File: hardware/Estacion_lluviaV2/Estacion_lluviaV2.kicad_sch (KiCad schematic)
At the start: 0 parts

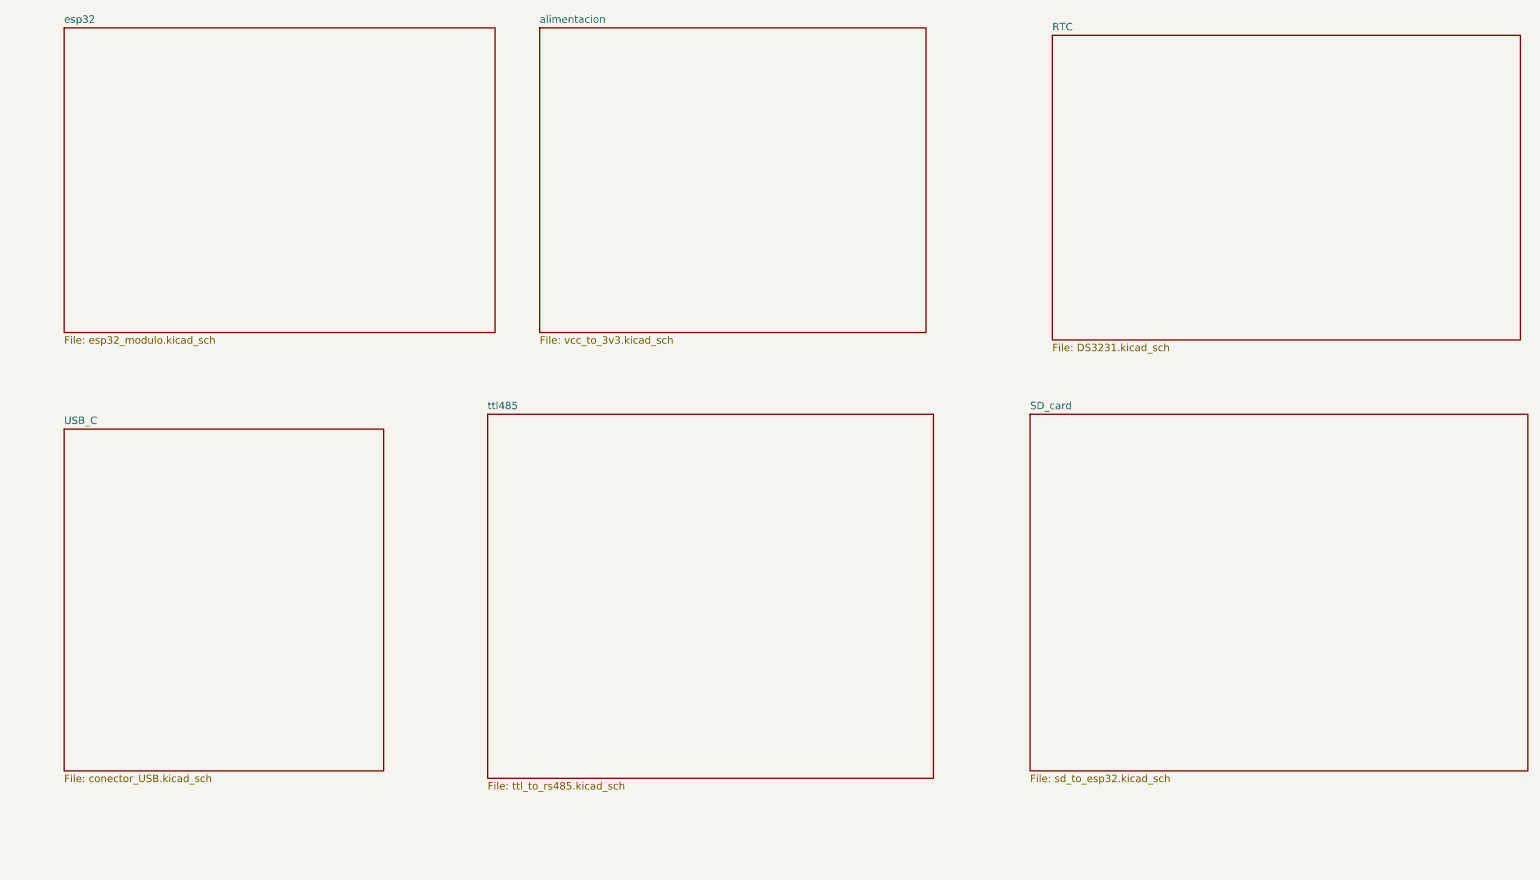
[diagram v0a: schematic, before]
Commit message: Se agregaron nuevos archivos
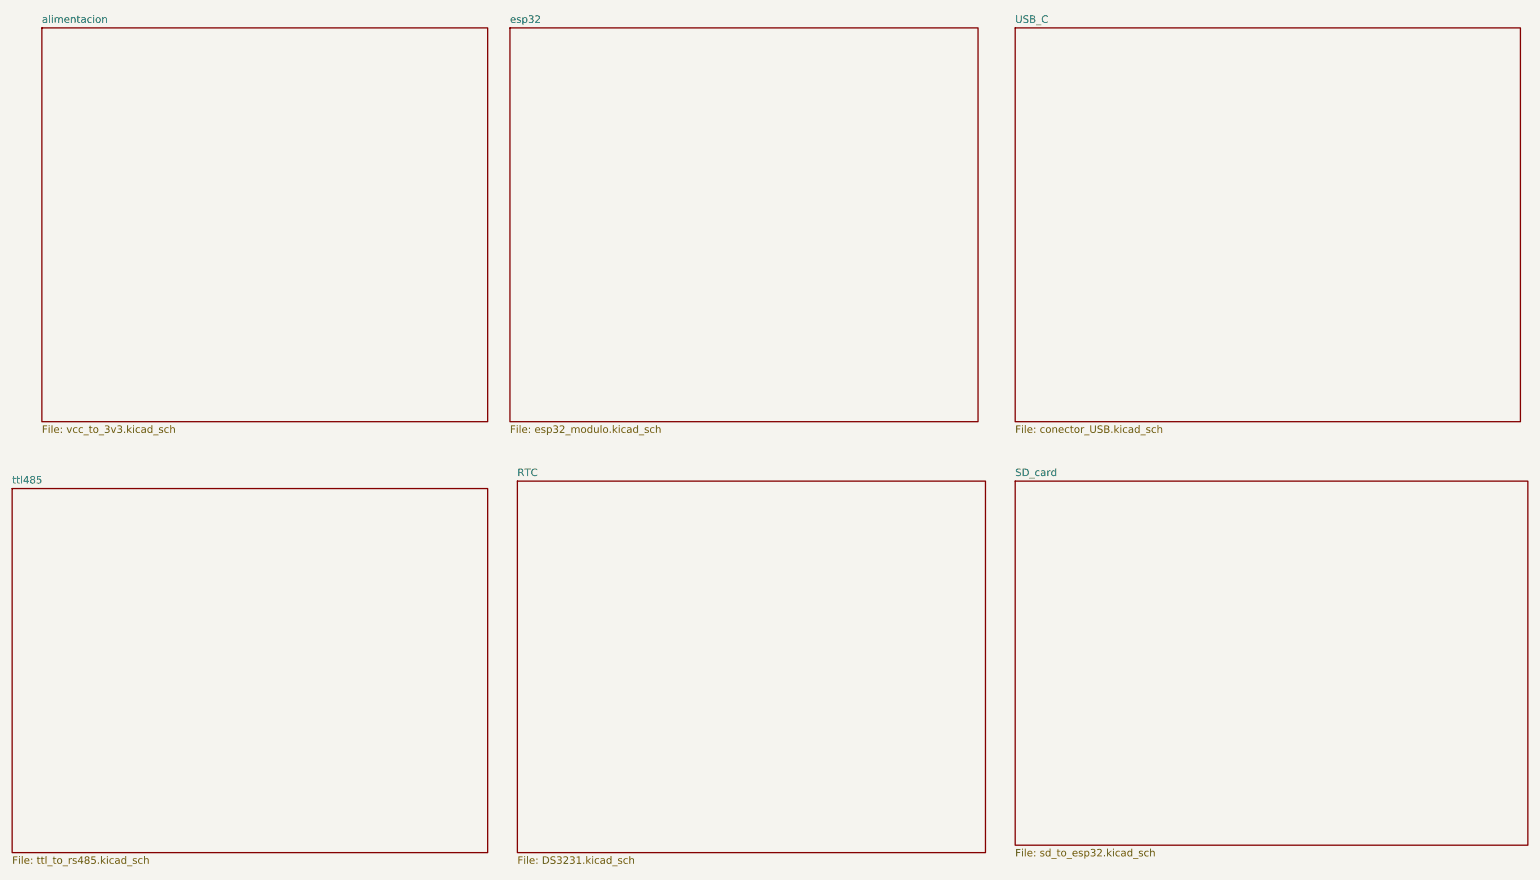
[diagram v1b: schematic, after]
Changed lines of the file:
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@@
 	(paper "A4")
 	(sheet
-		(at 22.86 88.9)
-		(size 54.61 58.42)
+		(at 185.42 20.32)
+		(size 86.36 67.31)
 		(exclude_from_sim no)
 		(in_bom yes)
@@
 		)
 		(property "Sheetname" "USB_C"
-			(at 22.86 88.1884 0)
+			(at 185.42 19.6084 0)
 			(effects
 				(font
@@
 		)
 		(property "Sheetfile" "conector_USB.kicad_sch"
-			(at 22.86 147.9046 0)
+			(at 185.42 88.2146 0)
 			(effects
 				(font
@@
 		)
 		(property "Field2" ""
-			(at 22.86 88.9 0)
+			(at 185.42 20.32 0)
 			(effects
 				(font
@@
 		)
 		(instances
-			(project "Estacion_lluvia"
+			(project "Estacion_lluviaV2"
+				(path "/9827a92f-f203-4536-a02d-33745fae0e99"
+					(page "4")
+				)
+			)
+		)
+	)
+	(sheet
+		(at 185.42 97.79)
+		(size 87.63 62.23)
+		(exclude_from_sim no)
+		(in_bom yes)
+		(on_board yes)
+		(dnp no)
+		(fields_autoplaced yes)
+		(stroke
+			(width 0.1524)
+			(type solid)
+		)
+		(fill
+			(color 0 0 0 0.0000)
+		)
+		(property "Sheetname" "SD_card"
+			(at 185.42 97.0784 0)
+			(effects
+				(font
+					(size 1.27 1.27)
+				)
+				(justify left bottom)
+			)
+		)
+		(property "Sheetfile" "sd_to_esp32.kicad_sch"
+			(at 185.42 160.6046 0)
+			(effects
+				(font
+					(size 1.27 1.27)
+				)
+				(justify left top)
+			)
+		)
+		(instances
+			(project "Estacion_lluviaV2"
 				(path "/9827a92f-f203-4536-a02d-33745fae0e99"
 					(page "7")
@@
 	)
 	(sheet
-		(at 187.96 86.36)
-		(size 85.09 60.96)
-		(exclude_from_sim no)
-		(in_bom yes)
-		(on_board yes)
-		(dnp no)
-		(fields_autoplaced yes)
-		(stroke
-			(width 0.1524)
-			(type solid)
-		)
-		(fill
-			(color 0 0 0 0.0000)
-		)
-		(property "Sheetname" "SD_card"
-			(at 187.96 85.6484 0)
-			(effects
-				(font
-					(size 1.27 1.27)
-				)
-				(justify left bottom)
-			)
-		)
-		(property "Sheetfile" "sd_to_esp32.kicad_sch"
-			(at 187.96 147.9046 0)
-			(effects
-				(font
-					(size 1.27 1.27)
-				)
-				(justify left top)
-			)
-		)
-		(instances
-			(project "Estacion_lluvia"
+		(at 99.06 20.32)
+		(size 80.01 67.31)
+		(exclude_from_sim no)
+		(in_bom yes)
+		(on_board yes)
+		(dnp no)
+		(fields_autoplaced yes)
+		(stroke
+			(width 0.1524)
+			(type solid)
+		)
+		(fill
+			(color 0 0 0 0.0000)
+		)
+		(property "Sheetname" "esp32"
+			(at 99.06 19.6084 0)
+			(effects
+				(font
+					(size 1.27 1.27)
+				)
+				(justify left bottom)
+			)
+		)
+		(property "Sheetfile" "esp32_modulo.kicad_sch"
+			(at 99.06 88.2146 0)
+			(effects
+				(font
+					(size 1.27 1.27)
+				)
+				(justify left top)
+			)
+		)
+		(instances
+			(project "Estacion_lluviaV2"
 				(path "/9827a92f-f203-4536-a02d-33745fae0e99"
 					(page "3")
@@
 	)
 	(sheet
-		(at 22.86 20.32)
-		(size 73.66 52.07)
-		(exclude_from_sim no)
-		(in_bom yes)
-		(on_board yes)
-		(dnp no)
-		(fields_autoplaced yes)
-		(stroke
-			(width 0.1524)
-			(type solid)
-		)
-		(fill
-			(color 0 0 0 0.0000)
-		)
-		(property "Sheetname" "esp32"
-			(at 22.86 19.6084 0)
-			(effects
-				(font
-					(size 1.27 1.27)
-				)
-				(justify left bottom)
-			)
-		)
-		(property "Sheetfile" "esp32_modulo.kicad_sch"
-			(at 22.86 72.9746 0)
-			(effects
-				(font
-					(size 1.27 1.27)
-				)
-				(justify left top)
-			)
-		)
-		(instances
-			(project "Estacion_lluvia"
-				(path "/9827a92f-f203-4536-a02d-33745fae0e99"
-					(page "4")
-				)
-			)
-		)
-	)
-	(sheet
-		(at 104.14 20.32)
-		(size 66.04 52.07)
+		(at 19.05 20.32)
+		(size 76.2 67.31)
 		(exclude_from_sim no)
 		(in_bom yes)
@@
 		)
 		(property "Sheetname" "alimentacion"
-			(at 104.14 19.6084 0)
+			(at 19.05 19.6084 0)
 			(effects
 				(font
@@
 		)
 		(property "Sheetfile" "vcc_to_3v3.kicad_sch"
-			(at 104.14 72.9746 0)
-			(effects
-				(font
-					(size 1.27 1.27)
-				)
-				(justify left top)
-			)
-		)
-		(instances
-			(project "Estacion_lluvia"
+			(at 19.05 88.2146 0)
+			(effects
+				(font
+					(size 1.27 1.27)
+				)
+				(justify left top)
+			)
+		)
+		(instances
+			(project "Estacion_lluviaV2"
+				(path "/9827a92f-f203-4536-a02d-33745fae0e99"
+					(page "2")
+				)
+			)
+		)
+	)
+	(sheet
+		(at 100.33 97.79)
+		(size 80.01 63.5)
+		(exclude_from_sim no)
+		(in_bom yes)
+		(on_board yes)
+		(dnp no)
+		(fields_autoplaced yes)
+		(stroke
+			(width 0.1524)
+			(type solid)
+		)
+		(fill
+			(color 0 0 0 0.0000)
+		)
+		(property "Sheetname" "RTC"
+			(at 100.33 97.0784 0)
+			(effects
+				(font
+					(size 1.27 1.27)
+				)
+				(justify left bottom)
+			)
+		)
+		(property "Sheetfile" "DS3231.kicad_sch"
+			(at 100.33 161.8746 0)
+			(effects
+				(font
+					(size 1.27 1.27)
+				)
+				(justify left top)
+			)
+		)
+		(instances
+			(project "Estacion_lluviaV2"
+				(path "/9827a92f-f203-4536-a02d-33745fae0e99"
+					(page "6")
+				)
+			)
+		)
+	)
+	(sheet
+		(at 13.97 99.06)
+		(size 81.28 62.23)
+		(exclude_from_sim no)
+		(in_bom yes)
+		(on_board yes)
+		(dnp no)
+		(fields_autoplaced yes)
+		(stroke
+			(width 0.1524)
+			(type solid)
+		)
+		(fill
+			(color 0 0 0 0.0000)
+		)
+		(property "Sheetname" "ttl485"
+			(at 13.97 98.3484 0)
+			(effects
+				(font
+					(size 1.27 1.27)
+				)
+				(justify left bottom)
+			)
+		)
+		(property "Sheetfile" "ttl_to_rs485.kicad_sch"
+			(at 13.97 161.8746 0)
+			(effects
+				(font
+					(size 1.27 1.27)
+				)
+				(justify left top)
+			)
+		)
+		(instances
+			(project "Estacion_lluviaV2"
 				(path "/9827a92f-f203-4536-a02d-33745fae0e99"
 					(page "5")
 				)
 			)
-		)
-	)
-	(sheet
-		(at 191.77 21.59)
-		(size 80.01 52.07)
-		(exclude_from_sim no)
-		(in_bom yes)
-		(on_board yes)
-		(dnp no)
-		(fields_autoplaced yes)
-		(stroke
-			(width 0.1524)
-			(type solid)
-		)
-		(fill
-			(color 0 0 0 0.0000)
-		)
-		(property "Sheetname" "RTC"
-			(at 191.77 20.8784 0)
-			(effects
-				(font
-					(size 1.27 1.27)
-				)
-				(justify left bottom)
-			)
-		)
-		(property "Sheetfile" "DS3231.kicad_sch"
-			(at 191.77 74.2446 0)
-			(effects
-				(font
-					(size 1.27 1.27)
-				)
-				(justify left top)
-			)
-		)
-		(instances
-			(project "Estacion_lluvia"
-				(path "/9827a92f-f203-4536-a02d-33745fae0e99"
-					(page "6")
-				)
-			)
-		)
-	)
-	(sheet
-		(at 95.25 86.36)
-		(size 76.2 62.23)
-		(exclude_from_sim no)
-		(in_bom yes)
-		(on_board yes)
-		(dnp no)
-		(fields_autoplaced yes)
-		(stroke
-			(width 0.1524)
-			(type solid)
-		)
-		(fill
-			(color 0 0 0 0.0000)
-		)
-		(property "Sheetname" "ttl485"
-			(at 95.25 85.6484 0)
-			(effects
-				(font
-					(size 1.27 1.27)
-				)
-				(justify left bottom)
-			)
-		)
-		(property "Sheetfile" "ttl_to_rs485.kicad_sch"
-			(at 95.25 149.1746 0)
-			(effects
-				(font
-					(size 1.27 1.27)
-				)
-				(justify left top)
-			)
-		)
-		(instances
-			(project "Estacion_lluvia"
-				(path "/9827a92f-f203-4536-a02d-33745fae0e99"
-					(page "2")
-				)
-			)
